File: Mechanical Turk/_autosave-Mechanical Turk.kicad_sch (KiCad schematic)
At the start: 6 parts, among them J1 Conn_01x01_Pin

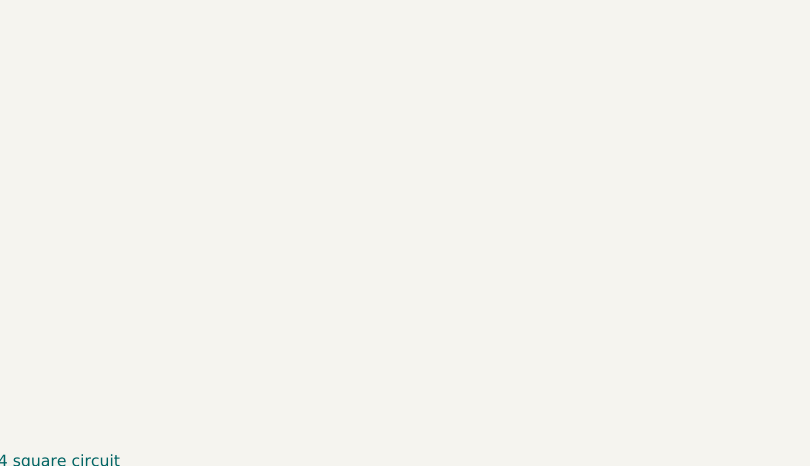
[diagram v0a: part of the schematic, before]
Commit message: removed cv folder
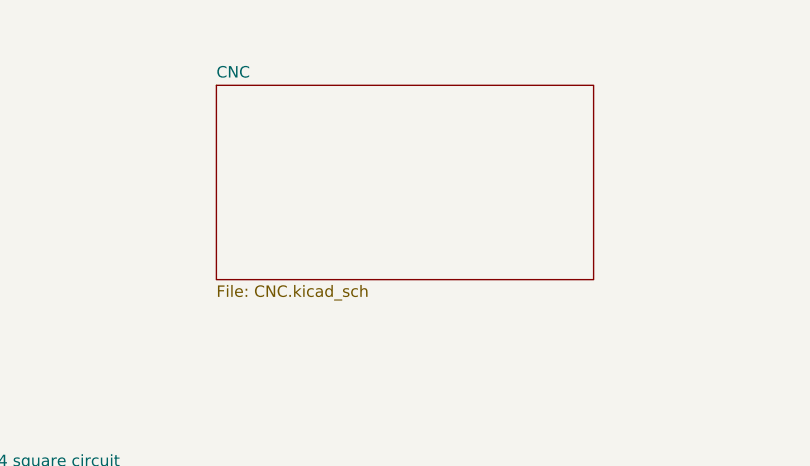
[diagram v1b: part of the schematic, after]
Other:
- added sheet CNC (CNC.kicad_sch)
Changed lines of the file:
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@@
+		)
+	)
+	(sheet
+		(at 161.29 22.86)
+		(size 41.91 21.59)
+		(fields_autoplaced yes)
+		(stroke
+			(width 0.1524)
+			(type solid)
+		)
+		(fill
+			(color 0 0 0 0.0000)
+		)
+		(property "Sheetname" "CNC"
+			(at 161.29 22.1484 0)
+			(effects
+				(font
+					(size 1.27 1.27)
+				)
+				(justify left bottom)
+			)
+		)
+		(property "Sheetfile" "CNC.kicad_sch"
+			(at 161.29 45.0346 0)
+			(effects
+				(font
+					(size 1.27 1.27)
+				)
+				(justify left top)
+			)
+		)
+		(instances
+			(project "Mechanical Turk"
+				(path "/7a1cc36f-228e-4763-bdcf-fd4d5555fb01"
+					(page "4")
+				)
+			)
 		)
 	)
